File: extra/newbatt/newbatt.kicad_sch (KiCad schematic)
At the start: 33 parts, among them J1 DC050-T, J2 Conn_01x05_MountingPin, U1 BQ24210DQCR, U5 XC6210B332MR

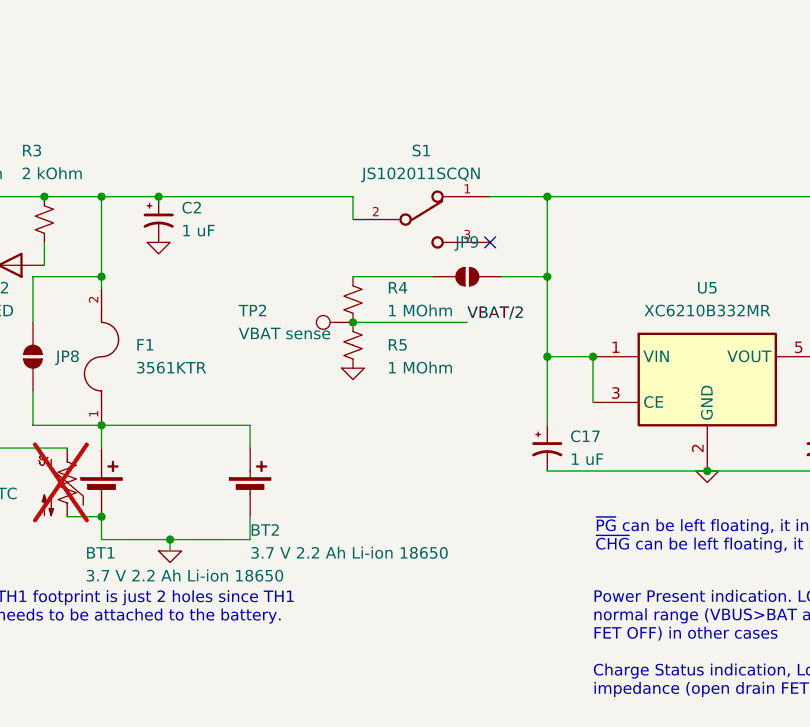
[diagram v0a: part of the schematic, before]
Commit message: updated battery footprint and slide switch
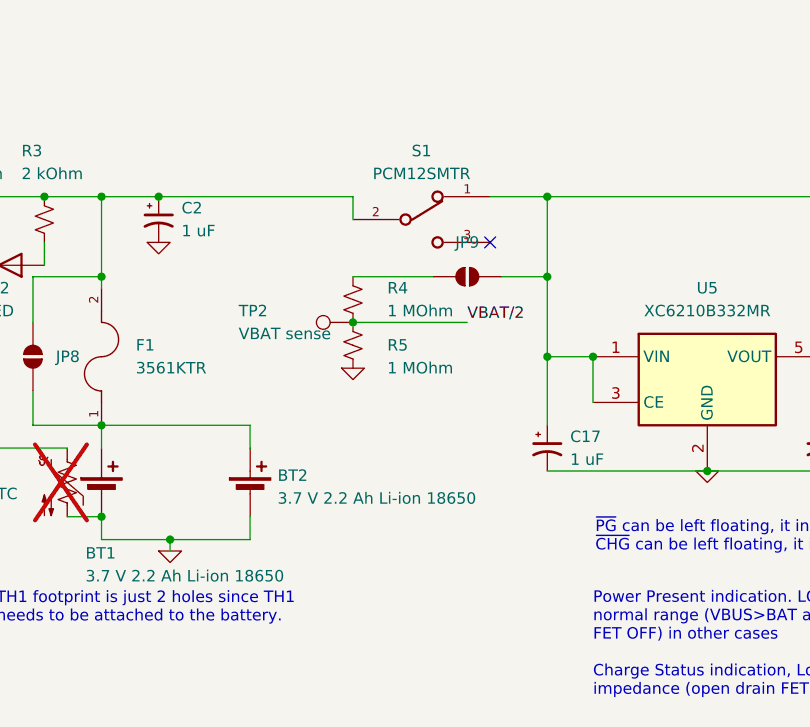
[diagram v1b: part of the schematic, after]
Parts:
- BT1, BT2: footprint Keystone254TR:BAT_254TR_67mm -> footprints:MY-18650-02; Digikey 36-254TR-ND -> (none); LCSC C5498533 -> C2979182; MFC Keystone -> MYOUNG; MPN 254TR -> MY-18650-02
- S1: value JS102011SCQN -> PCM12SMTR; footprint JS102011SCQN:SWITCH_1SCQN -> Button_Switch_SMD:SW_SPDT_PCM12; Digikey 401-1999-2-ND -> 401-2016-2-ND; LCSC C221660 -> C221841; MPN JS102011SAQN -> PCM12SMTR
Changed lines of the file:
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@@
-	)
-	(symbol
-		(lib_id "Device:Battery_Cell")
-		(at 148.59 101.6 0)
-		(unit 1)
-		(exclude_from_sim no)
-		(in_bom yes)
-		(on_board yes)
-		(dnp no)
-		(property "Reference" "BT2"
-			(at 148.59 105.664 0)
-			(effects
-				(font
-					(size 1.27 1.27)
-				)
-				(justify left)
-			)
-		)
-		(property "Value" "3.7 V 2.2 Ah Li-ion 18650"
-			(at 148.59 108.204 0)
-			(effects
-				(font
-					(size 1.27 1.27)
-				)
-				(justify left)
-			)
-		)
-		(property "Footprint" "Keystone254TR:BAT_254TR_67mm"
-			(at 148.59 100.076 90)
-			(effects
-				(font
-					(size 1.27 1.27)
-				)
-				(hide yes)
-			)
-		)
-		(property "Datasheet" "https://www.keyelco.com/product-pdf.cfm?p=14420"
-			(at 148.59 100.076 90)
-			(effects
-				(font
-					(size 1.27 1.27)
-				)
-				(hide yes)
-			)
-		)
-		(property "Description" "Single-cell battery"
-			(at 148.59 101.6 0)
-			(effects
-				(font
-					(size 1.27 1.27)
-				)
-				(hide yes)
-			)
-		)
-		(property "MFC" "Keystone"
-			(at 148.59 101.6 0)
-			(effects
-				(font
-					(size 1.27 1.27)
-				)
-				(hide yes)
-			)
-		)
-		(property "MPN" "254TR"
-			(at 148.59 101.6 0)
-			(effects
-				(font
-					(size 1.27 1.27)
-				)
-				(hide yes)
-			)
-		)
-		(property "QTY" "4"
-			(at 148.59 101.6 0)
-			(effects
-				(font
-					(size 1.27 1.27)
-				)
-				(hide yes)
-			)
-		)
-		(property "REF" "BT1, BT2"
-			(at 148.59 101.6 0)
-			(effects
-				(font
-					(size 1.27 1.27)
-				)
-				(hide yes)
-			)
-		)
-		(property "SNAPEDA_PACKAGE_ID" ""
-			(at 148.59 101.6 0)
-			(effects
-				(font
-					(size 1.27 1.27)
-				)
-				(hide yes)
-			)
-		)
-		(property "Digikey" "36-254TR-ND"
-			(at 148.59 101.6 0)
-			(effects
-				(font
-					(size 1.27 1.27)
-				)
-				(hide yes)
-			)
-		)
-		(property "LCSC" "C5498533"
-			(at 148.59 101.6 0)
-			(effects
-				(font
-					(size 1.27 1.27)
-				)
-				(hide yes)
-			)
-		)
-		(pin "1"
-		)
-		(pin "2"
-		)
-		(instances
-			(project "newbatt"
-				(path "/492e8d1d-dcc5-45c6-a3d2-2dfd8a06477e"
-					(reference "BT2")
-					(unit 1)
-				)
-			)
-		)
 	)
 	(symbol
@@
 			)
 		)
-		(property "Value" "JS102011SCQN"
+		(property "Value" "PCM12SMTR"
 			(at 167.64 66.04 0)
 			(effects
@@
 			)
 		)
-		(property "Footprint" "JS102011SCQN:SWITCH_1SCQN"
+		(property "Footprint" "Button_Switch_SMD:SW_SPDT_PCM12"
 			(at 167.64 71.12 0)
 			(effects
@@
 			)
 		)
-		(property "Datasheet" "https://www.ckswitches.com/media/1422/js.pdf"
+		(property "Datasheet" "https://www.ckswitches.com/media/1424/pcm.pdf"
 			(at 167.64 71.12 0)
 			(effects
@@
 			)
 		)
-		(property "MPN" "JS102011SAQN"
+		(property "MPN" "PCM12SMTR"
 			(at 167.64 71.12 0)
 			(effects
@@
 			)
 		)
-		(property "Digikey" "401-1999-2-ND"
+		(property "Digikey" "401-2016-2-ND"
 			(at 167.64 71.12 0)
 			(effects
@@
 			)
 		)
-		(property "LCSC" "C221660"
+		(property "LCSC" "C221841"
 			(at 167.64 71.12 0)
 			(effects
@@
 	)
 	(symbol
+		(lib_id "Device:Battery_Cell")
+		(at 148.59 101.6 0)
+		(unit 1)
+		(exclude_from_sim no)
+		(in_bom yes)
+		(on_board yes)
+		(dnp no)
+		(property "Reference" "BT2"
+			(at 151.638 99.568 0)
+			(effects
+				(font
+					(size 1.27 1.27)
+				)
+				(justify left)
+			)
+		)
+		(property "Value" "3.7 V 2.2 Ah Li-ion 18650"
+			(at 151.638 102.108 0)
+			(effects
+				(font
+					(size 1.27 1.27)
+				)
+				(justify left)
+			)
+		)
+		(property "Footprint" "footprints:MY-18650-02"
+			(at 148.59 100.076 90)
+			(effects
+				(font
+					(size 1.27 1.27)
+				)
+				(hide yes)
+			)
+		)
+		(property "Datasheet" "https://jlcpcb.com/api/file/downloadByFileSystemAccessId/8589834392282828800"
+			(at 148.59 100.076 90)
+			(effects
+				(font
+					(size 1.27 1.27)
+				)
+				(hide yes)
+			)
+		)
+		(property "Description" "Single-cell battery"
+			(at 148.59 101.6 0)
+			(effects
+				(font
+					(size 1.27 1.27)
+				)
+				(hide yes)
+			)
+		)
+		(property "MFC" "MYOUNG"
+			(at 148.59 101.6 0)
+			(effects
+				(font
+					(size 1.27 1.27)
+				)
+				(hide yes)
+			)
+		)
+		(property "MPN" "MY-18650-02"
+			(at 148.59 101.6 0)
+			(effects
+				(font
+					(size 1.27 1.27)
+				)
+				(hide yes)
+			)
+		)
+		(property "QTY" "4"
+			(at 148.59 101.6 0)
+			(effects
+				(font
+					(size 1.27 1.27)
+				)
+				(hide yes)
+			)
+		)
+		(property "REF" "BT1, BT2"
+			(at 148.59 101.6 0)
+			(effects
+				(font
+					(size 1.27 1.27)
+				)
+				(hide yes)
+			)
+		)
+		(property "SNAPEDA_PACKAGE_ID" ""
+			(at 148.59 101.6 0)
+			(effects
+				(font
+					(size 1.27 1.27)
+				)
+				(hide yes)
+			)
+		)
+		(property "Digikey" ""
+			(at 148.59 101.6 0)
+			(effects
+				(font
+					(size 1.27 1.27)
+				)
+				(hide yes)
+			)
+		)
+		(property "LCSC" "C2979182"
+			(at 148.59 101.6 0)
+			(effects
+				(font
+					(size 1.27 1.27)
+				)
+				(hide yes)
+			)
+		)
+		(pin "1"
+		)
+		(pin "2"
+		)
+		(instances
+			(project "newbatt"
+				(path "/492e8d1d-dcc5-45c6-a3d2-2dfd8a06477e"
+					(reference "BT2")
+					(unit 1)
+				)
+			)
+		)
+	)
+	(symbol
 		(lib_id "Connector_Generic_MountingPin:Conn_01x05_MountingPin")
 		(at 234.95 71.12 0)
@@
 			)
 		)
-		(property "Footprint" "Keystone254TR:BAT_254TR_67mm"
+		(property "Footprint" "footprints:MY-18650-02"
 			(at 132.08 100.076 90)
 			(effects
@@
 			)
 		)
-		(property "Datasheet" "https://www.keyelco.com/product-pdf.cfm?p=14420"
+		(property "Datasheet" "https://jlcpcb.com/api/file/downloadByFileSystemAccessId/8589834392282828800"
 			(at 132.08 100.076 90)
 			(effects
@@
 			)
 		)
-		(property "MFC" "Keystone"
+		(property "MFC" "MYOUNG"
 			(at 132.08 101.6 0)
 			(effects
@@
 			)
 		)
-		(property "MPN" "254TR"
+		(property "MPN" "MY-18650-02"
 			(at 132.08 101.6 0)
 			(effects
@@
 			)
 		)
-		(property "Digikey" "36-254TR-ND"
+		(property "Digikey" ""
 			(at 132.08 101.6 0)
 			(effects
@@
 			)
 		)
-		(property "LCSC" "C5498533"
+		(property "LCSC" "C2979182"
 			(at 132.08 101.6 0)
 			(effects
